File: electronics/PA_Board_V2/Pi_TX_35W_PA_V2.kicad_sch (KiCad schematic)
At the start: 6 parts

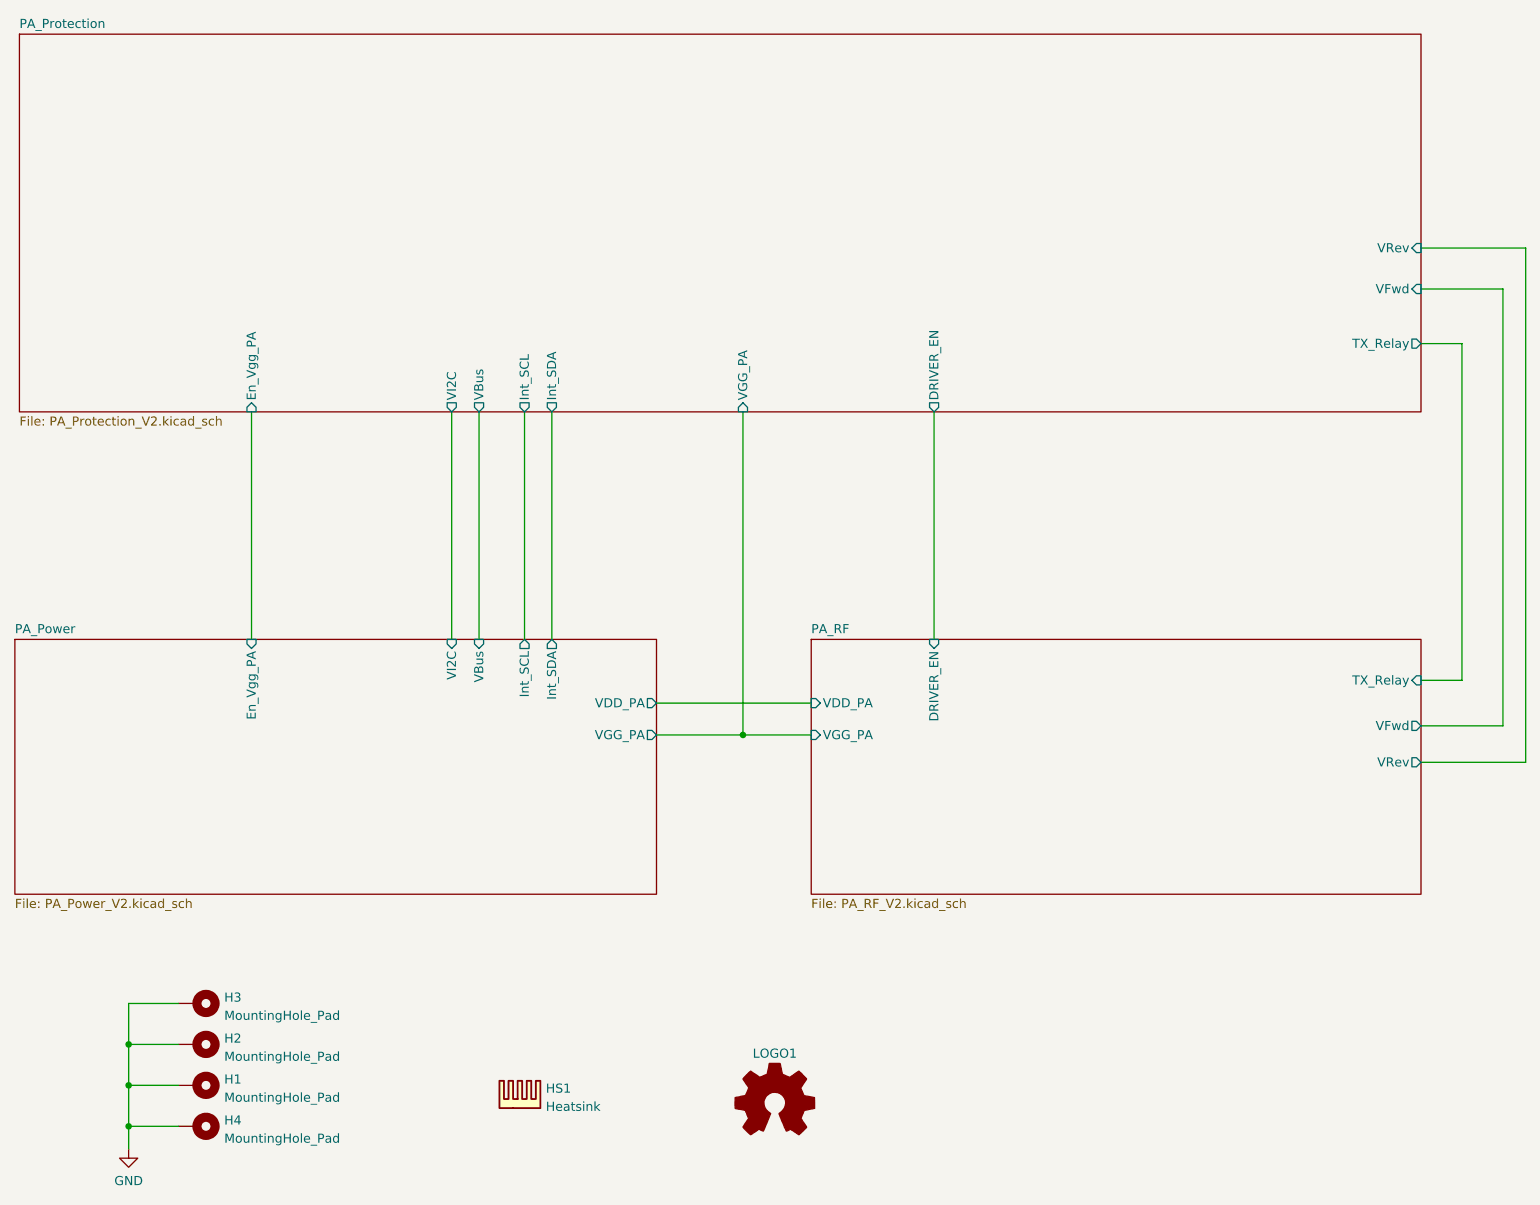
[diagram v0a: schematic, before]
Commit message: Update Arduino documentation and change to Kicad V8
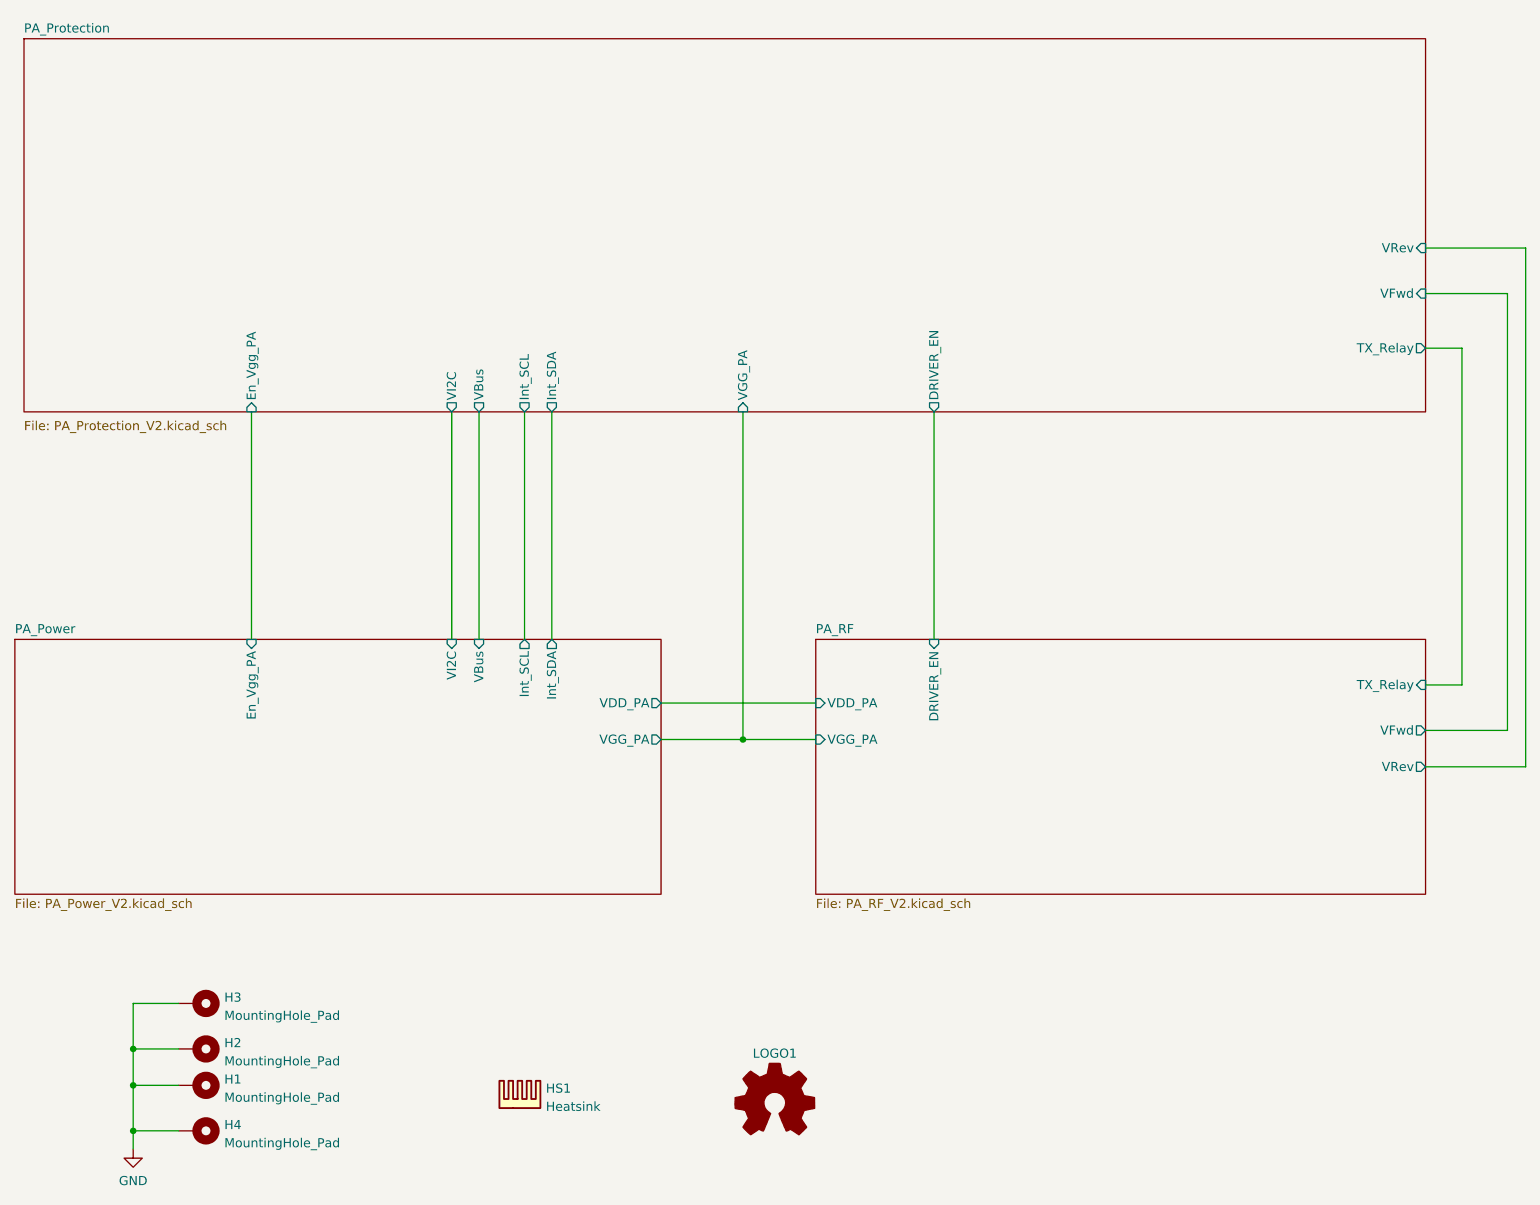
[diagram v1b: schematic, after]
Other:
- moved on the sheet: H2, H4
